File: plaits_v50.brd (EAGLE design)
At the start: 59 x 106.7 mm, 162 parts, among them IC1 R-78E3.3-0.5, IC2 TLC59281DBQ, IC3 LD2981ABU33, IC4 STM32F373CCT6, IC5 PCM5100APW, IC6 MCP6004, IC7 MCP6004, IC8 TL072PW, IC9 LM4040B10, J1 PJ301_THONKICONN6, J10 PJ301_THONKICONN6, J2 PJ301_THONKICONN6, J3 PJ301_THONKICONN6, J4 PJ301_THONKICONN6, J5 PJ301_THONKICONN6, J6 PJ301_THONKICONN6, J7 PJ301_THONKICONN6, J8 PJ301_THONKICONN6, J9 PJ301_THONKICONN6, Q1 8MHz

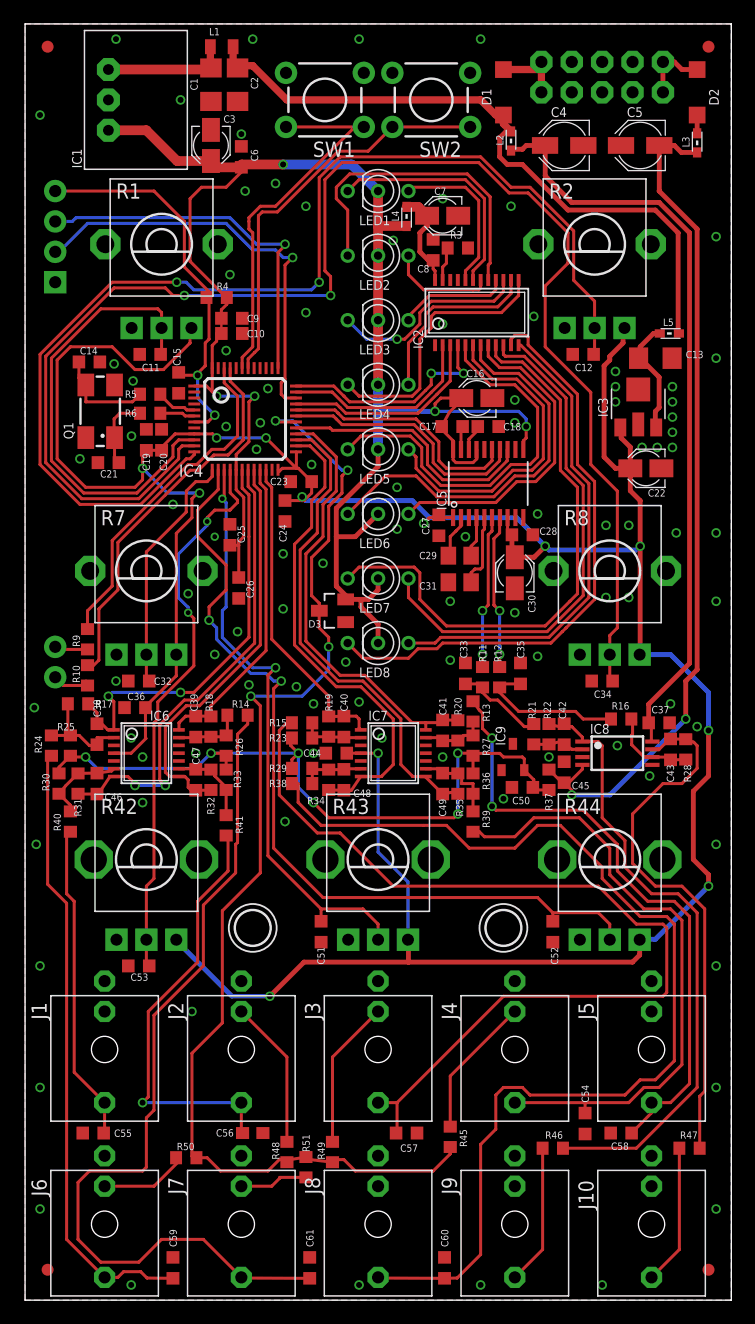
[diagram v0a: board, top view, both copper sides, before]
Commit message: Fixed tname positioning
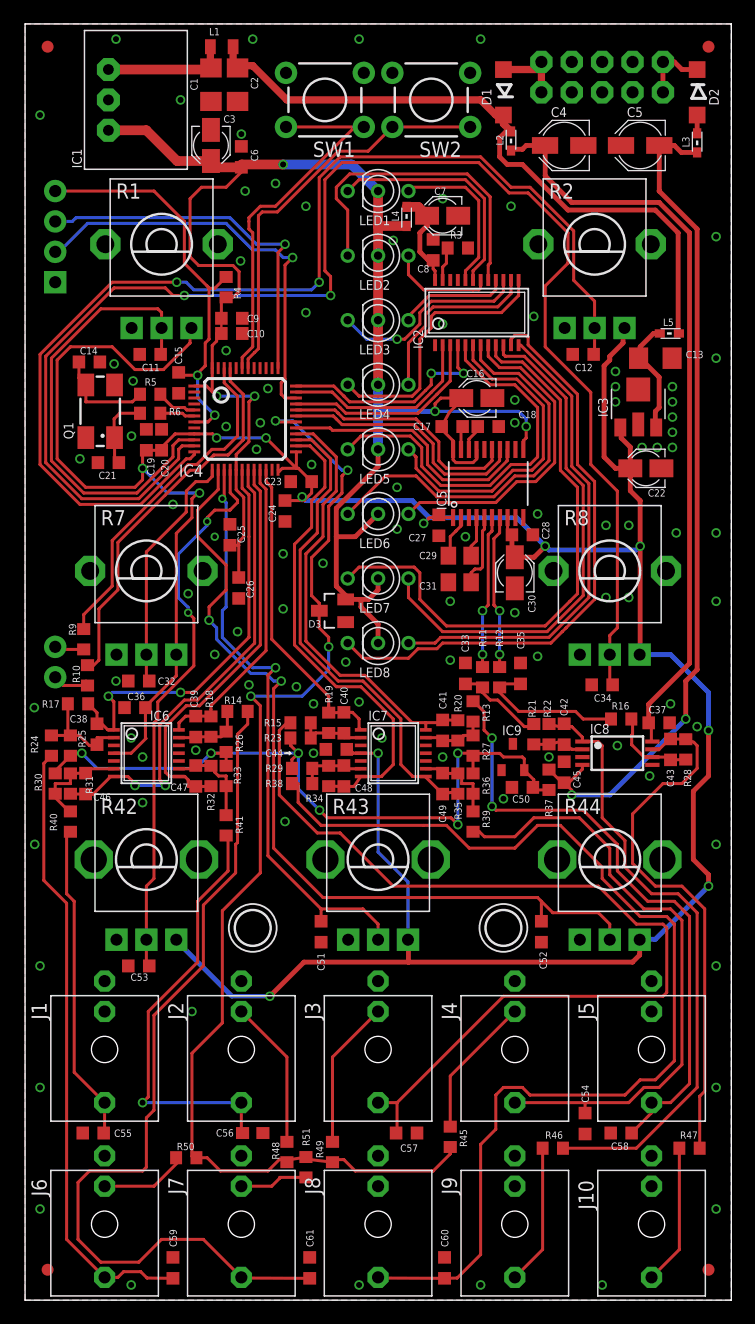
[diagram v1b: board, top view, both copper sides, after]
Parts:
- moved R4 1.17 mm to (16.8, 84.7), turned to 90 degrees
- moved C52 0.95 mm to (43.2, 30.8)
- moved C46 0.95 mm to (5.08, 43.2)
- moved R31 0.64 mm to (3.81, 43.2)
- moved C44 0.32 mm to (26.0, 46.0)
- moved R26 0.32 mm to (16.8, 46.7)
- moved R9 0.32 mm to (4.92, 55.2)
- moved R30 0.32 mm to (2.54, 43.2)
- moved C34 0.32 mm to (48.3, 51.4)
- moved C40 0.32 mm to (26.7, 48.3)
- moved C47 0.32 mm to (14.3, 43.8)
- moved C48 0.32 mm to (26.7, 43.8)
- moved R14 0.32 mm to (17.8, 49.2)
- moved R19 0.32 mm to (25.4, 48.3)
- moved R32 0.32 mm to (15.6, 43.8)
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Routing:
- net +3V3: track 150.9 -> 154.2 mm
- net RESET: track 33.7 -> 35.3 mm
- net N$37: track 7.29 -> 8.82 mm
- net AREF_-10: track 63.3 -> 64.5 mm
- net N$39: track 7.31 -> 8.30 mm
- net MORPH_ATT: track 70.5 -> 71.5 mm
- net N$34: track 5.42 -> 5.99 mm
